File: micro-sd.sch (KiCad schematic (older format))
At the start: 2 parts

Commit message: sch, lib: Upgrade to KiCAD 5.1.0
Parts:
- removed J?: Micro_SD_Card_Det, symbol Connector:Micro_SD_Card_Det
- added J?: Micro_SD_Card_Det, symbol Connector:Micro_SD_Card_Det
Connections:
- net +3V3: now also J?.4 (VDD)
- net GND: now also J?.11 (SHIELD), J?.6 (VSS)
- net SD_CLK: now also J?.5 (CLK)
- net SD_CMD: now also J?.3 (CMD)
- net SD_D0: now also J?.7 (DAT0)
- net SD_D1: now also J?.8 (DAT1)
- net SD_D2: now also J?.1 (DAT2)
- net SD_D3: now also J?.2 (DAT3/CD)
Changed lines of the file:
@@
 EESchema Schematic File Version 4
 LIBS:pimouss-motherboard-cache
-EELAYER 26 0
+EELAYER 29 0
 EELAYER END
 $Descr A4 11693 8268
 encoding utf-8
-Sheet 9 13
+Sheet 12 13
 Title "µSD Card storage"
 Date "2019-03-19"
@@
 Comment4 ""
 $EndDescr
-$Comp
-L Connector:Micro_SD_Card_Det J?
-U 1 1 5D0A2A6B
-P 5750 3850
-F 0 "J?" H 5700 4667 50  0000 C CNN
-F 1 "Micro_SD_Card_Det" H 5700 4576 50  0000 C CNN
-F 2 "" H 7800 4550 50  0001 C CNN
-F 3 "https://www.hirose.com/product/en/download_file/key_name/DM3/category/Catalog/doc_file_id/49662/?file_category_id=4&item_id=195&is_series=1" H 5750 3950 50  0001 C CNN
-	1    5750 3850
-	1    0    0    -1
-$EndComp
 $Comp
 L power:+3V3 #PWR?
@@
 Wire Bus Line
 	4000 3350 4000 4050
+$Comp
+L Connector:Micro_SD_Card_Det J?
+U 1 1 5C97B7D0
+P 5750 3850
+F 0 "J?" H 5700 4667 50  0000 C CNN
+F 1 "Micro_SD_Card_Det" H 5700 4576 50  0000 C CNN
+F 2 "" H 7800 4550 50  0001 C CNN
+F 3 "https://www.hirose.com/product/en/download_file/key_name/DM3/category/Catalog/doc_file_id/49662/?file_category_id=4&item_id=195&is_series=1" H 5750 3950 50  0001 C CNN
+	1    5750 3850
+	1    0    0    -1
+$EndComp
 $EndSCHEMATC

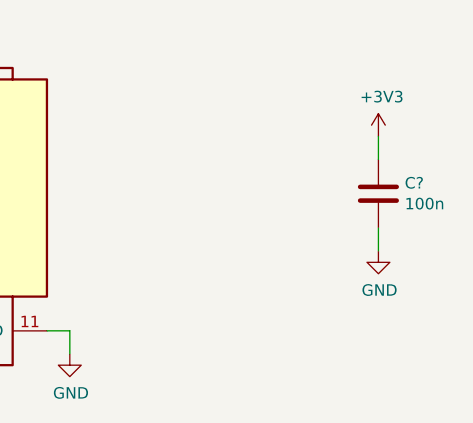
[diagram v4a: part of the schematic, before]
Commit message: sch: Replace regular symbols with small variant
Done for most capacitors and resistors
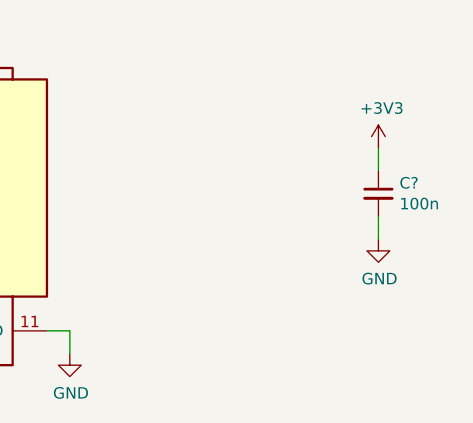
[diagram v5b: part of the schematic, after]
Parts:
- removed C?: 100n, symbol Device:C
- added C?: 100n, symbol Device:C_Small
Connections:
- net +3V3: now also C?.1
- net GND: now also C?.2
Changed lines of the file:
@@
 SDIO
-$Comp
-L Device:C C?
-U 1 1 5D0AFC43
-P 8000 3750
-F 0 "C?" H 8115 3796 50  0000 L CNN
-F 1 "100n" H 8115 3705 50  0000 L CNN
-F 2 "" H 8038 3600 50  0001 C CNN
-F 3 "~" H 8000 3750 50  0001 C CNN
-	1    8000 3750
-	1    0    0    -1
-$EndComp
 $Comp
 L power:GND #PWR?
 U 1 1 5D0AFE08
-P 8000 4000
-F 0 "#PWR?" H 8000 3750 50  0001 C CNN
-F 1 "GND" H 8005 3827 50  0000 C CNN
-F 2 "" H 8000 4000 50  0001 C CNN
-F 3 "" H 8000 4000 50  0001 C CNN
-	1    8000 4000
+P 8000 3950
+F 0 "#PWR?" H 8000 3700 50  0001 C CNN
+F 1 "GND" H 8005 3777 50  0000 C CNN
+F 2 "" H 8000 3950 50  0001 C CNN
+F 3 "" H 8000 3950 50  0001 C CNN
+	1    8000 3950
 	1    0    0    -1
 $EndComp
@@
 L power:+3V3 #PWR?
 U 1 1 5D0AFE1C
-P 8000 3500
-F 0 "#PWR?" H 8000 3350 50  0001 C CNN
-F 1 "+3V3" H 8015 3673 50  0000 C CNN
-F 2 "" H 8000 3500 50  0001 C CNN
-F 3 "" H 8000 3500 50  0001 C CNN
-	1    8000 3500
+P 8000 3550
+F 0 "#PWR?" H 8000 3400 50  0001 C CNN
+F 1 "+3V3" H 8015 3723 50  0000 C CNN
+F 2 "" H 8000 3550 50  0001 C CNN
+F 3 "" H 8000 3550 50  0001 C CNN
+	1    8000 3550
 	1    0    0    -1
 $EndComp
 Wire Wire Line
-	8000 3500 8000 3600
+	8000 3550 8000 3650
 Wire Wire Line
-	8000 3900 8000 4000
+	8000 3850 8000 3950
 $Comp
 L Connector:Micro_SD_Card_Det J?
@@
 	1    0    0    -1
 $EndComp
+$Comp
+L Device:C_Small C?
+U 1 1 5D4AB31A
+P 8000 3750
+F 0 "C?" H 8092 3796 50  0000 L CNN
+F 1 "100n" H 8092 3705 50  0000 L CNN
+F 2 "" H 8000 3750 50  0001 C CNN
+F 3 "~" H 8000 3750 50  0001 C CNN
+	1    8000 3750
+	1    0    0    -1
+$EndComp

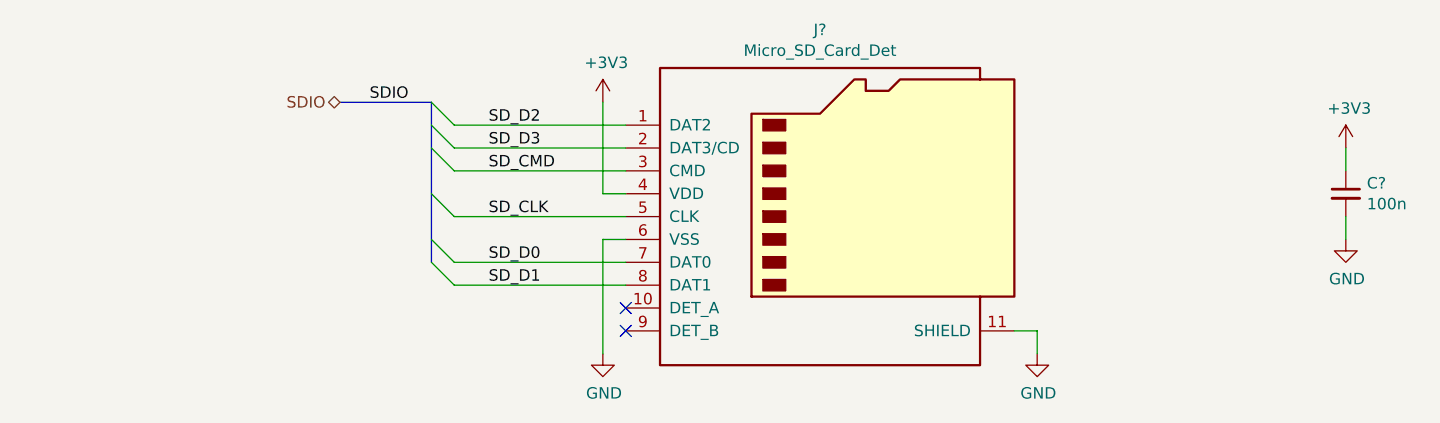
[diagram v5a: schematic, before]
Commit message: sch: Remove ALL busses since kicad's support is broken
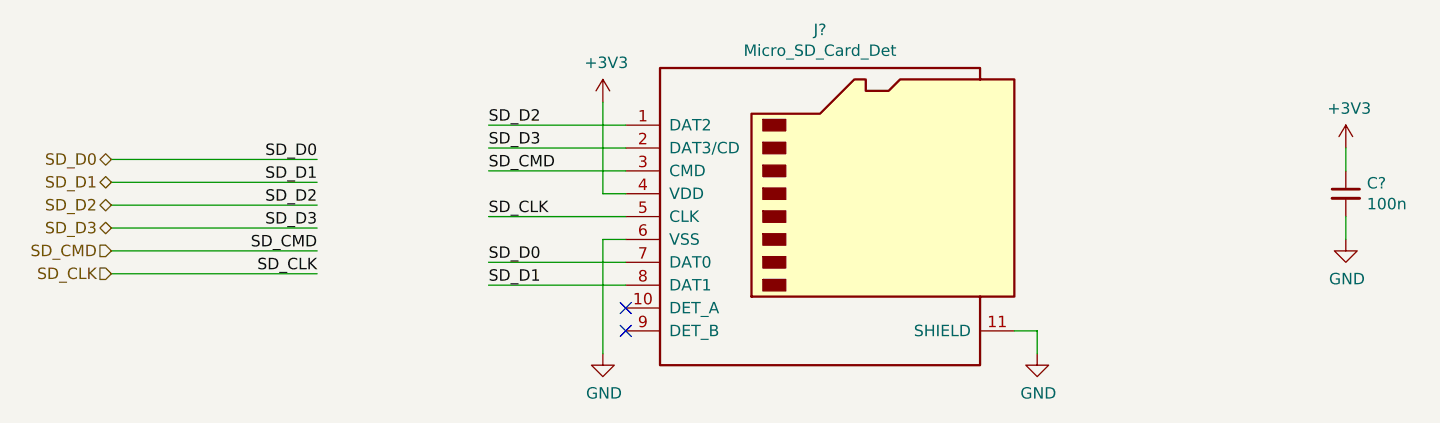
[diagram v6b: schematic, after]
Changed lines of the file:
@@
 $EndComp
 Wire Wire Line
-	4850 3650 4100 3650
+	4850 3650 4250 3650
 Wire Wire Line
-	4850 3850 4100 3850
+	4850 3850 4250 3850
 Wire Wire Line
-	4850 3450 4100 3450
+	4850 3450 4250 3450
 Wire Wire Line
-	4850 3550 4100 3550
+	4850 3550 4250 3550
 Wire Wire Line
-	4850 4150 4100 4150
+	4850 4150 4250 4150
 Wire Wire Line
-	4850 4050 4100 4050
+	4850 4050 4250 4050
 Text Label 4250 3650 0    50   ~ 0
 SD_CMD
@@
 Text Label 4250 4050 0    50   ~ 0
 SD_D0
-Wire Bus Line
-	3600 3350 4000 3350
-Text Label 3900 3350 2    50   ~ 0
-SDIO
-Entry Wire Line
-	4100 3650 4000 3550
-Entry Wire Line
-	4100 4050 4000 3950
-Entry Wire Line
-	4100 3450 4000 3350
-Entry Wire Line
-	4100 3550 4000 3450
-Entry Wire Line
-	4100 3850 4000 3750
-Entry Wire Line
-	4100 4150 4000 4050
 NoConn ~ 4850 4250
 NoConn ~ 4850 4350
-Text HLabel 3600 3350 0    50   BiDi ~ 0
-SDIO
 $Comp
 L power:GND #PWR?
@@
 	1    0    0    -1
 $EndComp
-Wire Bus Line
-	4000 3350 4000 4050
+Wire Wire Line
+	3500 3800 2600 3800
+Wire Wire Line
+	3500 3900 2600 3900
+Text Label 3500 3800 2    50   ~ 0
+SD_D2
+Text Label 3500 3900 2    50   ~ 0
+SD_D3
+Wire Wire Line
+	3500 3700 2600 3700
+Wire Wire Line
+	3500 3600 2600 3600
+Text Label 3500 3700 2    50   ~ 0
+SD_D1
+Text Label 3500 3600 2    50   ~ 0
+SD_D0
+Wire Wire Line
+	2600 4000 3500 4000
+Wire Wire Line
+	2600 4100 3500 4100
+Text Label 3500 4000 2    50   ~ 0
+SD_CMD
+Text Label 3500 4100 2    50   ~ 0
+SD_CLK
+Text HLabel 2600 4000 0    50   Input ~ 0
+SD_CMD
+Text HLabel 2600 4100 0    50   Input ~ 0
+SD_CLK
+Text HLabel 2600 3800 0    50   BiDi ~ 0
+SD_D2
+Text HLabel 2600 3900 0    50   BiDi ~ 0
+SD_D3
+Text HLabel 2600 3700 0    50   BiDi ~ 0
+SD_D1
+Text HLabel 2600 3600 0    50   BiDi ~ 0
+SD_D0
 $EndSCHEMATC

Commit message: sch: Annotate & associate symbols with footprints
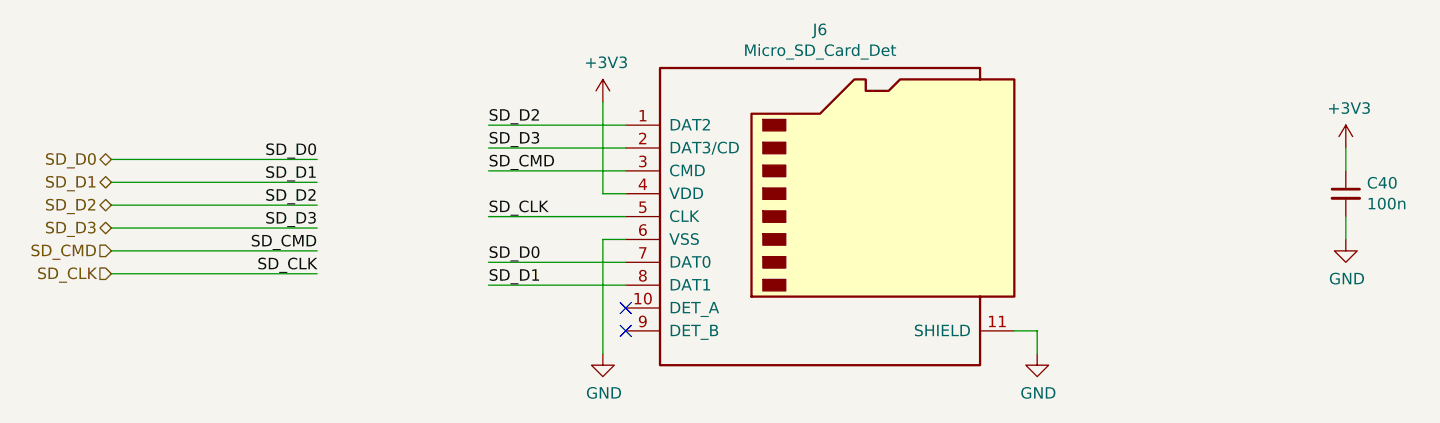
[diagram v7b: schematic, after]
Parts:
- C40: renamed from C?; footprint (none) -> Capacitor_SMD:C_0603_1608Metric
- J6: renamed from J?; footprint (none) -> Connector_Card:microSD_HC_Hirose_DM3D-SF
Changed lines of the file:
@@
 $EndDescr
 $Comp
-L power:+3V3 #PWR?
+L power:+3V3 #PWR090
 U 1 1 5D0A2BBF
 P 4750 3350
-F 0 "#PWR?" H 4750 3200 50  0001 C CNN
+F 0 "#PWR090" H 4750 3200 50  0001 C CNN
 F 1 "+3V3" H 4765 3523 50  0000 C CNN
 F 2 "" H 4750 3350 50  0001 C CNN
@@
 	6650 4350 6650 4450
 $Comp
-L power:GND #PWR?
+L power:GND #PWR091
 U 1 1 5D0A2C0D
 P 4750 4450
-F 0 "#PWR?" H 4750 4200 50  0001 C CNN
+F 0 "#PWR091" H 4750 4200 50  0001 C CNN
 F 1 "GND" H 4755 4277 50  0000 C CNN
 F 2 "" H 4750 4450 50  0001 C CNN
@@
 $EndComp
 $Comp
-L power:GND #PWR?
+L power:GND #PWR092
 U 1 1 5D0A2C31
 P 6650 4450
-F 0 "#PWR?" H 6650 4200 50  0001 C CNN
+F 0 "#PWR092" H 6650 4200 50  0001 C CNN
 F 1 "GND" H 6655 4277 50  0000 C CNN
 F 2 "" H 6650 4450 50  0001 C CNN
@@
 NoConn ~ 4850 4350
 $Comp
-L power:GND #PWR?
+L power:GND #PWR094
 U 1 1 5D0AFE08
 P 8000 3950
-F 0 "#PWR?" H 8000 3700 50  0001 C CNN
+F 0 "#PWR094" H 8000 3700 50  0001 C CNN
 F 1 "GND" H 8005 3777 50  0000 C CNN
 F 2 "" H 8000 3950 50  0001 C CNN
@@
 $EndComp
 $Comp
-L power:+3V3 #PWR?
+L power:+3V3 #PWR093
 U 1 1 5D0AFE1C
 P 8000 3550
-F 0 "#PWR?" H 8000 3400 50  0001 C CNN
+F 0 "#PWR093" H 8000 3400 50  0001 C CNN
 F 1 "+3V3" H 8015 3723 50  0000 C CNN
 F 2 "" H 8000 3550 50  0001 C CNN
@@
 	8000 3850 8000 3950
 $Comp
-L Connector:Micro_SD_Card_Det J?
+L Connector:Micro_SD_Card_Det J6
 U 1 1 5C97B7D0
 P 5750 3850
-F 0 "J?" H 5700 4667 50  0000 C CNN
+F 0 "J6" H 5700 4667 50  0000 C CNN
 F 1 "Micro_SD_Card_Det" H 5700 4576 50  0000 C CNN
-F 2 "" H 7800 4550 50  0001 C CNN
+F 2 "Connector_Card:microSD_HC_Hirose_DM3D-SF" H 7800 4550 50  0001 C CNN
 F 3 "https://www.hirose.com/product/en/download_file/key_name/DM3/category/Catalog/doc_file_id/49662/?file_category_id=4&item_id=195&is_series=1" H 5750 3950 50  0001 C CNN
 	1    5750 3850
@@
 $EndComp
 $Comp
-L Device:C_Small C?
+L Device:C_Small C40
 U 1 1 5D4AB31A
 P 8000 3750
-F 0 "C?" H 8092 3796 50  0000 L CNN
+F 0 "C40" H 8092 3796 50  0000 L CNN
 F 1 "100n" H 8092 3705 50  0000 L CNN
-F 2 "" H 8000 3750 50  0001 C CNN
+F 2 "Capacitor_SMD:C_0603_1608Metric" H 8000 3750 50  0001 C CNN
 F 3 "~" H 8000 3750 50  0001 C CNN
 	1    8000 3750

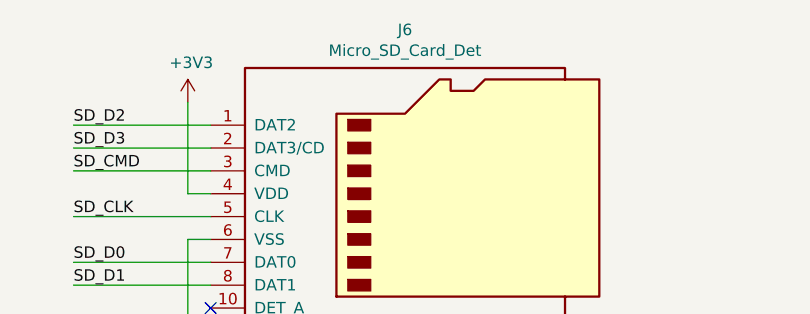
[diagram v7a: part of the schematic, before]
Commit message: lib, sch: Fix connectors refdes letter
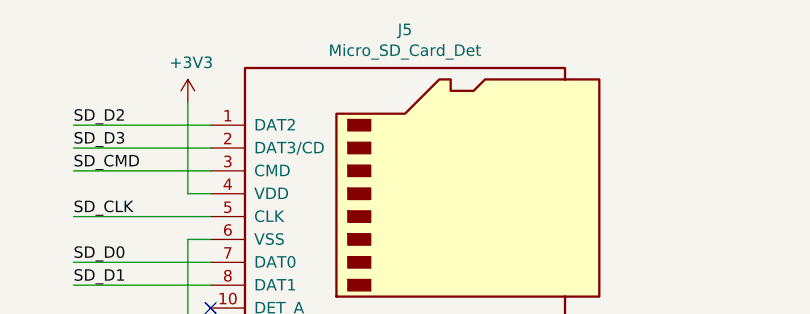
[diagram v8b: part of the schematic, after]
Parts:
- renumbered J6 to J5
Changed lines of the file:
@@
 	8000 3850 8000 3950
 $Comp
-L Connector:Micro_SD_Card_Det J6
+L Connector:Micro_SD_Card_Det J5
 U 1 1 5C97B7D0
 P 5750 3850
-F 0 "J6" H 5700 4667 50  0000 C CNN
+F 0 "J5" H 5700 4667 50  0000 C CNN
 F 1 "Micro_SD_Card_Det" H 5700 4576 50  0000 C CNN
 F 2 "Connector_Card:microSD_HC_Hirose_DM3D-SF" H 7800 4550 50  0001 C CNN
